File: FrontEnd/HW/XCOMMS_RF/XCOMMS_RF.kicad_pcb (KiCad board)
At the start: 2 copper layers, 40 x 65 mm, 82 parts, among them J1 SMA, J2 SMA, J3 SFC-110-T2-F-D-A-TR, U1 SIM-14+, U2 HMC788ALP2ETR, U3 HMC952ALP5GE, U4 LMX2572RHAT, U5 HMC788ALP2ETR, U6 AD8031, U7 ADT7310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

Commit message: XCOMMS_RF and XCOMMS_Interface KiCad design updated
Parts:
- C49: value Cap Semi -> 100nF
- C50: value Cap Semi -> 100pF
- C51: value Cap Semi -> 1uF
- R10, R7, R8, R9: value Res3 -> 10k
- R5, R6: value Res3 -> 100k
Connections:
- net Net-(C1-Pad1) renamed /AMP1_Out
- net Net-(C1-Pad2) renamed /TP2_In
- net Net-(C2-Pad1) renamed /TP1_Out
- net Net-(C2-Pad2) renamed /AMP1_In
- net Net-(C29-Pad1) renamed /PLL_Out
- net Net-(FL1-Pad1) renamed /Mixer_Out
- R10 pad 1: Net-(R10-Pad1) -> GND
- R10 pad 2: GND -> Net-(R10-Pad2)
- R7 pad 1: Net-(R7-Pad1) -> /Vdet
- R7 pad 2: /Vdet -> Net-(R7-Pad2)
- R8 pad 1: /Tx_PM -> Net-(R7-Pad2)
- R8 pad 2: Net-(R7-Pad1) -> /Tx_PM
- R9 pad 1: Net-(R10-Pad1) -> Net-(R10-Pad2)
- U6 pad 3: Net-(R10-Pad1) -> Net-(R10-Pad2)
- U6 pad 4: Net-(R7-Pad1) -> Net-(R7-Pad2)
- U6 pad 5: /5V -> +5V
- Y1 pad 1: /LO_EN -> /LocalOscillator/LO_EN
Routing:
- net Net-(R7-Pad1): track 9.87 -> 0.00 mm, vias 2 -> 0
- net /Vdet: track 26.6 -> 36.4 mm, vias 2 -> 4
- net Net-(R10-Pad2): track 0.00 -> 3.07 mm
- net Net-(R10-Pad1): track 3.07 -> 0.00 mm

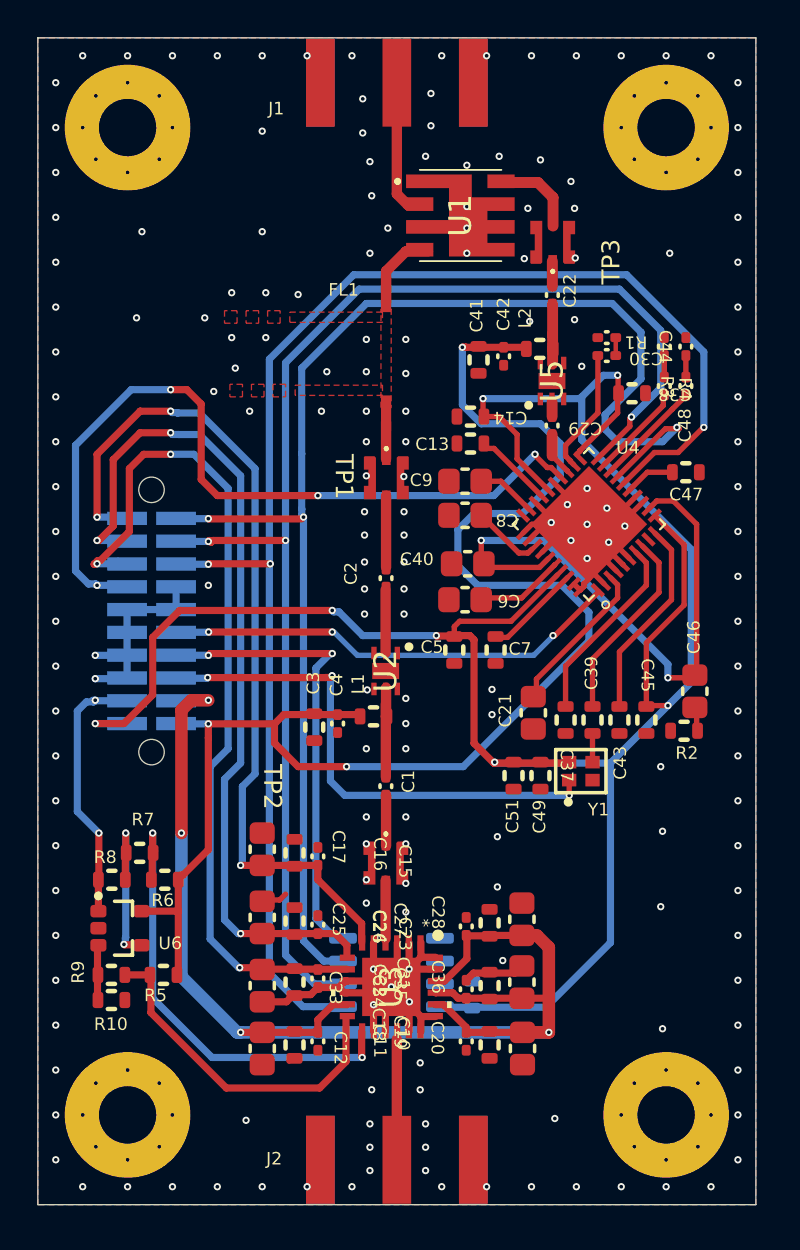
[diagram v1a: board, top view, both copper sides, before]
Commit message: XCOMMS_RF ported to KiCad
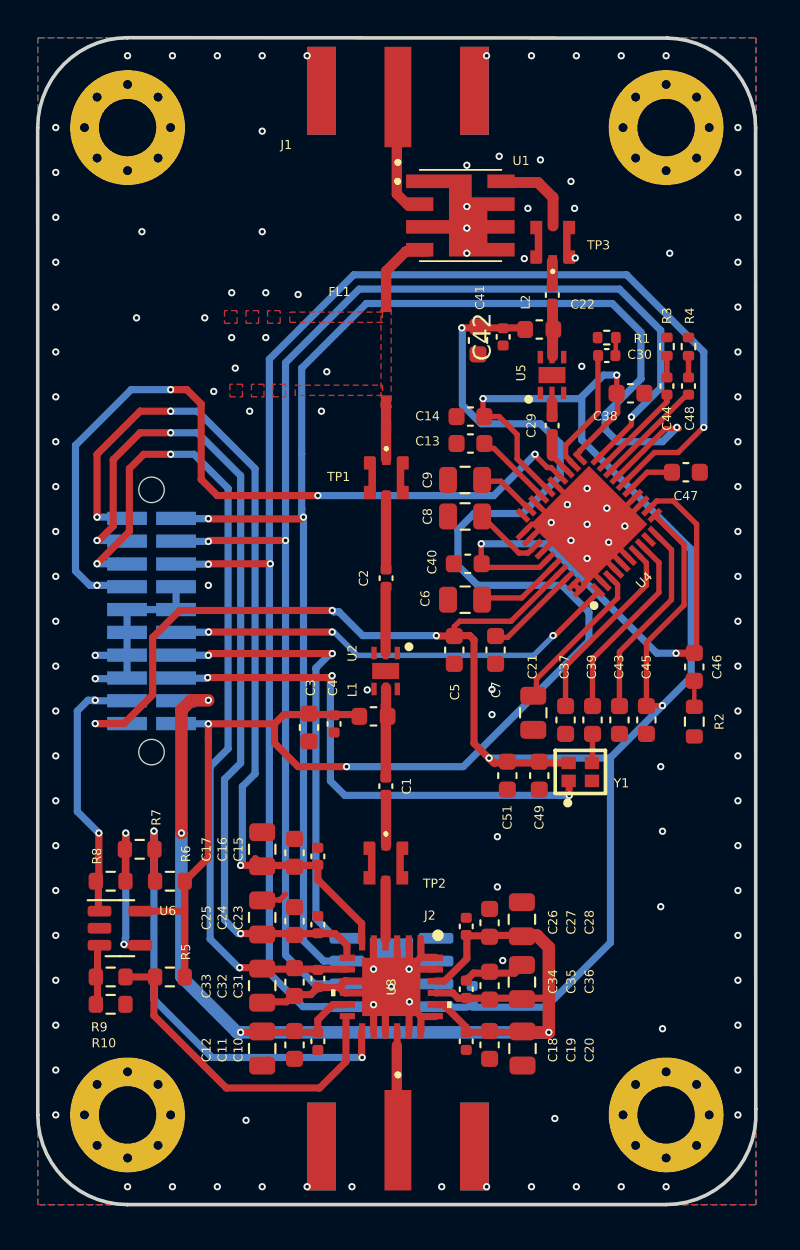
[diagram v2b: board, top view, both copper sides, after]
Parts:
- C1, C10, C15, C18, C2, C22, C23, C26, C31, C34, C4, C42: footprint 3CAT_Miscellaneous.PcbLib:0402 SND CAPACITOR -> Capacitor_SMD:C_0402_1005Metric
- C11, C13, C14, C16, C19, C24, C27, C3, C32, C35, C37, C38, C39, C41, C43, C45, C47, C49, C5, C51, C7: footprint 3CAT_Miscellaneous.PcbLib:0603 SMD Capacitor -> Capacitor_SMD:C_0603_1608Metric
- C12, C17, C20, C21, C25, C28, C33, C36, C6, C8, C9: footprint 3CAT_Miscellaneous.PcbLib:0805 SMD Capacitor -> Capacitor_SMD:C_0805_2012Metric
- C29, C30, C44, C48: value 100nF -> 100pF; footprint 3CAT_Miscellaneous.PcbLib:0402 SND CAPACITOR -> Capacitor_SMD:C_0402_1005Metric
- C40, C46: footprint 3CAT_Miscellaneous.PcbLib:0805 SMD Capacitor -> Capacitor_SMD:C_0603_1608Metric
- C50: footprint 3CAT_Miscellaneous.PcbLib:0603 SMD Capacitor -> Capacitor_SMD:C_0402_1005Metric
- J1, J2: footprint Connectors_GGS.PcbLib:CONSMA020-062-G -> GGS_Connectors:LINX_CONSMA020.062-G
- J3: footprint Connectors_GGS.PcbLib:SAMTEC_SFC-110-T2-F-D-A-TR -> GGS_Connectors:SAMTEC_SFC-110-T2-F-D-A-TR
- L1, L2: footprint 3CAT_Miscellaneous.PcbLib:0603 SMD Inductor -> Inductor_SMD:L_0603_1608Metric
- R1, R3, R4: footprint 3CAT_Miscellaneous.PcbLib:0402 SMD Resistor -> Resistor_SMD:R_0402_1005Metric
- R10, R2, R5, R6, R7, R8, R9: footprint 3CAT_Miscellaneous.PcbLib:0603 SMD Resistor -> Resistor_SMD:R_0603_1608Metric
- SCRW1, SCRW2, SCRW3, SCRW4: footprint 3CAT_Miscellaneous.PcbLib:M3 ScrewHole -> MountingHole:MountingHole_3.2mm_M3_Pad_Via
- U4: footprint RF_GGS.PcbLib:QFN50P600X600X100-41N -> SamacSys_Footprints:QFN50P600X600X100-41N-D
- U6: footprint 3CAT_Miscellaneous.PcbLib:SOT-23-5 -> Package_TO_SOT_SMD:SOT-23-5
- U7: footprint 3CAT_Miscellaneous.PcbLib:SOIC-8 -> Package_SO:SOIC-8-1EP_3.9x4.9mm_P1.27mm_EP2.41x3.81mm
- Y1: footprint Miscellaneous_GGS.PcbLib:ECS-TXO-2016 -> GGS_Miscellaneous:TCXO_ECS
- moved Y1 5.12 mm to (162.2, 117.0)
- moved J1 4.65 mm to (152.7, 72.1)
- moved J2 4.65 mm to (152.7, 135.8)
- moved C46 1.36 mm to (169.2, 106.6)
- moved C42 1.08 mm to (158.6, 88.2)
- moved C41 1.08 mm to (157.2, 88.4)
- moved L2 1.08 mm to (160.6, 87.8)
- moved R2 0.76 mm to (169.2, 109.7), turned to -90 degrees
- moved R5 0.38 mm to (140.0, 123.9)
- moved C51 0.34 mm to (158.8, 112.7)
- moved U5 0.33 mm to (161.3, 90.3)
- moved R6 0.30 mm to (140.0, 118.5)
- moved C3 0.29 mm to (147.8, 110.0)
- moved R10 0.24 mm to (136.7, 125.4), turned to 180 degrees
- moved C4 0.20 mm to (149.1, 109.8)
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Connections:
- net Net-(C13-Pad2) renamed /LocalOscillator/VBIASVCO2
- net Net-(C21-Pad2) renamed /LocalOscillator/VBIASVCO
- net Net-(C22-Pad1) renamed /AMP2_Out
- net Net-(C22-Pad2) renamed /TP3_In
- net Net-(C30-Pad2) renamed /LocalOscillator/RFOUTAM
- net Net-(C39-Pad2) renamed /LocalOscillator/OSCINP
- net Net-(C40-Pad2) renamed /LocalOscillator/VTune
- net Net-(C43-Pad2) renamed /LocalOscillator/OSCINM
- net Net-(C44-Pad2) renamed /LocalOscillator/RFOUTBP
- net Net-(C48-Pad2) renamed /LocalOscillator/RFOUTBM
- net Net-(C6-Pad2) renamed /LocalOscillator/VREFVCO
- net Net-(C8-Pad2) renamed /LocalOscillator/VBIASVARAC
- net Net-(C9-Pad2) renamed /LocalOscillator/VREFVCO2
- net Net-(R10-Pad2) renamed /AD8031_IN+
- net Net-(R7-Pad2) renamed /AD8031_IN-
- C29 pad 1: /PLL_Out -> /LocalOscillator/RFOUTAP
- C29 pad 2: Net-(C29-Pad2) -> /PLL_Out
- U4 pad 23: Net-(C29-Pad2) -> /LocalOscillator/RFOUTAP
- Y1 pad 1: /LocalOscillator/LO_EN -> /LO_EN
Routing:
- net /AD8031_IN-: track 0.00 -> 9.87 mm, vias 0 -> 2
- net /Vdet: track 36.4 -> 26.6 mm, vias 4 -> 2
- net /LocalOscillator/VTune: track 32.7 -> 30.2 mm
- net Net-(C29-Pad2): track 2.39 -> 0.00 mm
- net /LocalOscillator/RFOUTAP: track 0.00 -> 2.39 mm
- net +5V: track 83.7 -> 85.0 mm
- net GND: track 81.6 -> 80.7 mm, vias 219 -> 125
- net Net-(C46-Pad1): track 1.46 -> 0.95 mm
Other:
- outline, holes or cut-outs redrawn

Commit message: XCOMS_RF updated
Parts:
- removed FL1: NotchFilter, RF_GGS.PcbLib:Notch_5600to6100MHz
- C21: value 10uF -> 470nF
- C7: value 1uF -> 10nF
- moved C37 2.17 mm to (159.9, 109.6), turned to 0 degrees
- moved C5 1.81 mm to (156.6, 104.0), turned to 0 degrees
- moved C7 1.75 mm to (159.9, 105.5), turned to 0 degrees
- moved C21 1.70 mm to (159.6, 107.6), turned to 0 degrees
- moved TP3 1.38 mm to (166.4, 83.6)
- moved R1 0.92 mm to (165.1, 88.8), turned to -90 degrees
- moved C22 0.92 mm to (162.2, 85.6), turned to 45 degrees
- moved C40 0.78 mm to (156.6, 100.1)
- moved C6 0.75 mm to (156.5, 102.1)
- moved C30 0.70 mm to (163.8, 88.8), turned to -90 degrees
- moved C47 0.25 mm to (168.8, 96.0), turned to 90 degrees
- moved L1 0.09 mm to (151.3, 109.3)
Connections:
- net /Tx_CE renamed /PLL_CE
- net Net-(C7-Pad2) renamed /LocalOscillator/VREGVCO
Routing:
- net +3V3: track 147.5 -> 154.1 mm, vias 7 -> 8
- net /SDI: track 78.6 -> 76.4 mm
- net /AMP1_Out: track 5.69 -> 3.56 mm
- net /Vdet: track 26.6 -> 28.7 mm
- net /Mixer_Out: track 6.63 -> 4.79 mm
- net /Vref: track 18.8 -> 17.1 mm, vias 0 -> 2
- net /SCK: track 82.6 -> 81.5 mm
- net /AMP1_In: track 3.50 -> 2.41 mm
- net /TP2_In: track 2.83 -> 1.76 mm
- net GND: track 80.7 -> 81.8 mm, vias 125 -> 89
- net /Vd_PA: track 74.1 -> 73.1 mm
- net /TP1_Out: track 4.00 -> 3.05 mm
- net /LocalOscillator/VTune: track 30.2 -> 29.3 mm
- net /LocalOscillator/VREGVCO: track 5.39 -> 4.52 mm
- net /TP3_In: track 1.44 -> 0.76 mm
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
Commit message: XCOMMS_RF update
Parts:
- added FL1: HFCW-7000+, GGS_RF:JC0603C, F.Cu at (152.7, 88.8)
- moved C30 2.16 mm to (163.8, 90.9)
- moved C38 2.11 mm to (166.0, 89.3), turned to -90 degrees
- moved R1 1.27 mm to (163.8, 88.8), turned to 90 degrees
- moved C22 0.64 mm to (161.7, 86.0)
- moved C46 0.56 mm to (169.2, 106.0)
- moved TP3 0.38 mm to (166.0, 83.6)
- moved R7 0.20 mm to (138.3, 117.0)
- moved R2 0.18 mm to (169.2, 109.5)
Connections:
- net /RF_Tx_in renamed /RF_in
- net /RF_Tx_out renamed /RF_out
- TP1 pad 1: /Mixer_Out -> /FL_Out
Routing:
- net GND: track 81.8 -> 70.6 mm, vias 89 -> 88
- net /PLL_CSB: track 45.0 -> 36.4 mm
- net /FL_Out: track 0.00 -> 4.77 mm
- net /Vg_PA1: track 48.3 -> 43.7 mm
- net /Vg_PA2: track 47.8 -> 44.4 mm
- net /SDI: track 76.4 -> 73.5 mm
- net /SDO: track 75.5 -> 73.0 mm
- net /LocalOscillator/RFOUTAM: track 6.72 -> 4.29 mm
- net /Vg_PA3: track 47.7 -> 45.4 mm
- net /Tx_PM: track 15.0 -> 12.8 mm
- net /T_CSB: track 25.9 -> 23.9 mm
- net /SCK: track 81.5 -> 79.8 mm
- net /TP3_In: track 0.76 -> 2.24 mm
- net /Vdet: track 28.7 -> 27.5 mm
- net /PLL_CE: track 25.5 -> 26.6 mm
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- removed copper zone on F.Cu, net (none)
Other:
- board text added: "ROGERS 4350B Layers = 2 Metalization = 35 um Thinkness = 0.762 mm (30 mils) Er = 3.66 tand = 0.0037"

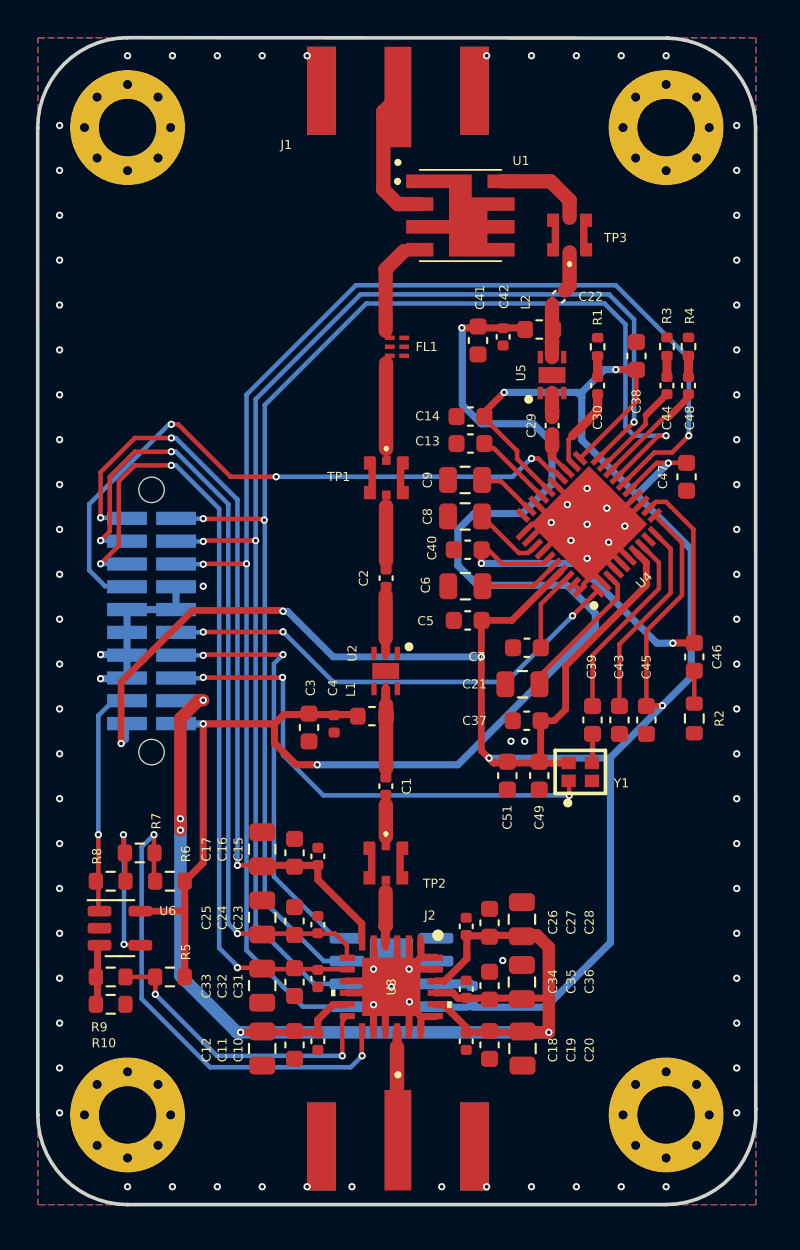
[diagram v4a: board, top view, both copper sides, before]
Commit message: Relaxed Design RUles and output files generated
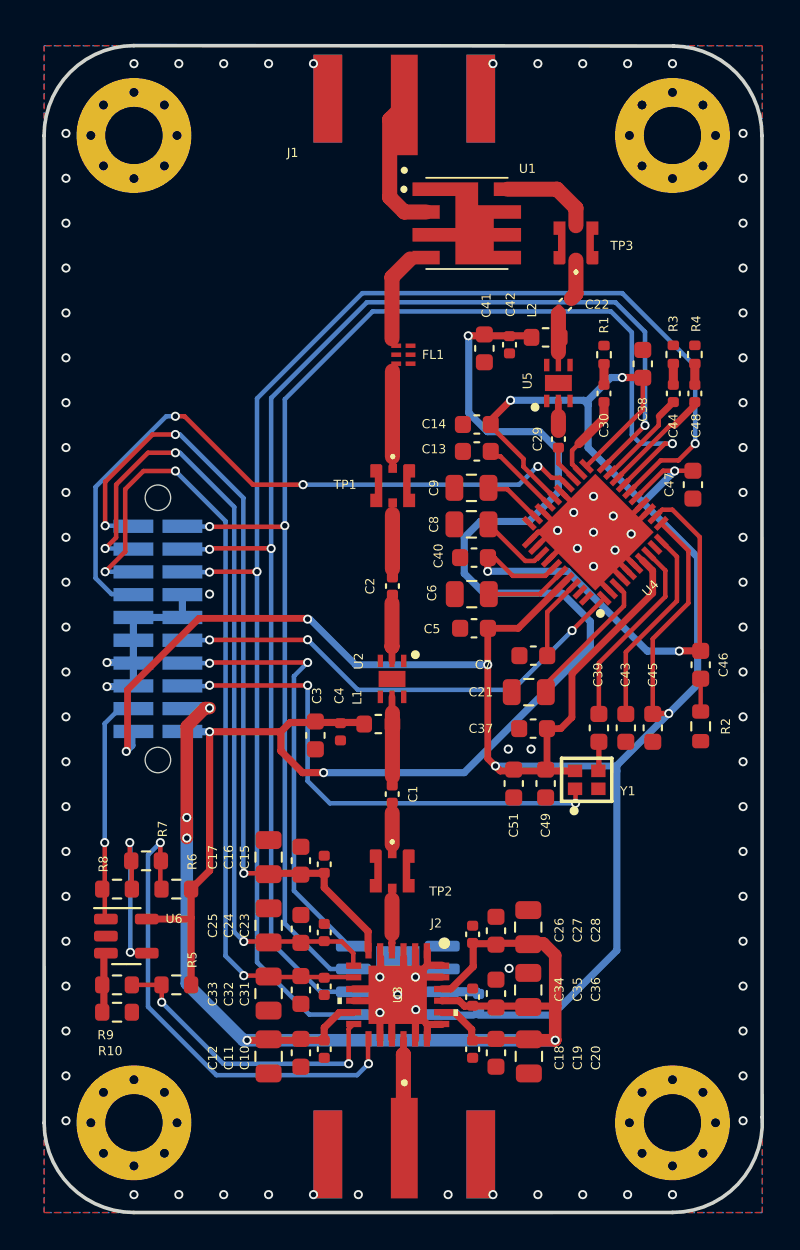
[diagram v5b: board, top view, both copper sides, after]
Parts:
- moved C29 0.83 mm to (161.6, 93.9)
- moved C2 0.57 mm to (152.4, 102.1)
- moved R6 0.57 mm to (140.4, 119.0)
- moved C16 0.57 mm to (147.3, 117.4)
- moved C24 0.57 mm to (147.3, 121.2)
- moved C27 0.57 mm to (158.2, 121.3)
- moved C35 0.57 mm to (158.2, 124.8)
- moved C41 0.57 mm to (157.5, 88.9)
- moved C47 0.57 mm to (169.1, 96.5)
- moved C8 0.57 mm to (156.8, 98.7)
- moved C9 0.57 mm to (156.8, 96.6)
- moved J3 0.57 mm to (139.3, 104.5)
- moved R5 0.57 mm to (140.4, 124.3)
- moved R7 0.57 mm to (138.7, 117.4)
- moved U1 0.57 mm to (156.5, 81.9)
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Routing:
- net GND: track 70.6 -> 68.7 mm
- net /PLL_CSB: track 36.4 -> 37.9 mm
- net /Vg_PA1: track 43.7 -> 44.7 mm
- net +5V: track 84.4 -> 83.5 mm
- net /LocalOscillator/RFOUTAP: track 2.51 -> 1.71 mm
- net /AMP2_Out: track 2.86 -> 2.16 mm
- net /PA_RF_IN: track 2.85 -> 3.50 mm
- net /FL_Out: track 4.77 -> 5.42 mm
- net /AMP1_Out: track 4.45 -> 5.08 mm
- net /LO_EN: track 28.3 -> 28.9 mm
- net /Vg_PA2: track 44.4 -> 45.0 mm
- net /T_CSB: track 23.9 -> 24.4 mm
- net /Vd_PA: track 74.0 -> 74.5 mm
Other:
- board text added: "ROGERS 4350B Layers = 2 Metalization = 35 um Thinkness = 0.508 mm (20 mils) Er = 3.66 tand = 0.0037"
- board text removed: "ROGERS 4350B Layers = 2 Metalization = 35 um Thinkness = 0.762 mm (30 mils) Er = 3.66 tand = 0.0037"

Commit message: changes
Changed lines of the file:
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@@
     (fp_line (start -0.14058 0.51) (end 0.14058 0.51) (layer "F.SilkS") (width 0.12))
     (fp_line (start -0.14058 -0.51) (end 0.14058 -0.51) (layer "F.SilkS") (width 0.12))
+    (fp_line (start -1.48 -0.73) (end 1.48 -0.73) (layer "F.CrtYd") (width 0.05))
     (fp_line (start -1.48 0.73) (end -1.48 -0.73) (layer "F.CrtYd") (width 0.05))
-    (fp_line (start 1.48 -0.73) (end 1.48 0.73) (layer "F.CrtYd") (width 0.05))
     (fp_line (start 1.48 0.73) (end -1.48 0.73) (layer "F.CrtYd") (width 0.05))
-    (fp_line (start -1.48 -0.73) (end 1.48 -0.73) (layer "F.CrtYd") (width 0.05))
+    (fp_line (start 1.48 -0.73) (end 1.48 0.73) (layer "F.CrtYd") (width 0.05))
     (fp_line (start -0.8 0.4) (end -0.8 -0.4) (layer "F.Fab") (width 0.1))
-    (fp_line (start -0.8 -0.4) (end 0.8 -0.4) (layer "F.Fab") (width 0.1))
     (fp_line (start 0.8 -0.4) (end 0.8 0.4) (layer "F.Fab") (width 0.1))
+    (fp_line (start -0.8 -0.4) (end 0.8 -0.4) (layer "F.Fab") (width 0.1))
     (fp_line (start 0.8 0.4) (end -0.8 0.4) (layer "F.Fab") (width 0.1))
     (pad "1" smd roundrect (at -0.775 0 270) (size 0.9 0.95) (layers "F.Cu" "F.Paste" "F.Mask") (roundrect_rratio 0.25)
@@
   (segment (start 147.420998 96.452) (end 144.626998 96.452) (width 0.254) (layer "F.Cu") (net 14))
   (segment (start 140.816998 92.642) (end 140.308998 92.642) (width 0.254) (layer "F.Cu") (net 14))
-  (segment (start 160.62623 95.436) (end 161.26123 96.071) (width 0.254) (layer "F.Cu") (net 14))
-  (segment (start 161.26123 96.071) (end 161.731669 96.071) (width 0.254) (layer "F.Cu") (net 14))
-  (segment (start 144.626998 96.452) (end 140.816998 92.642) (width 0.254) (layer "F.Cu") (net 14))
-  (segment (start 161.731669 96.071) (end 162.144375 96.483706) (width 0.254) (layer "F.Cu") (net 14))
+  (segment (start 161.20223 96.012) (end 161.672669 96.012) (width 0.254) (layer "F.Cu") (net 14))
+  (segment (start 160.62623 95.436) (end 161.20223 96.012) (width 0.254) (layer "F.Cu") (net 14))
   (segment (start 160.501998 95.436) (end 160.62623 95.436) (width 0.254) (layer "F.Cu") (net 14))
+  (segment (start 144.626998 96.452) (end 140.816998 92.642) (width 0.254) (layer "F.Cu") (net 14))
+  (segment (start 161.672669 96.012) (end 162.144375 96.483706) (width 0.254) (layer "F.Cu") (net 14))
   (via (at 160.501998 95.436) (size 0.508) (drill 0.3048) (layers "F.Cu" "B.Cu") (net 14))
   (via (at 140.308998 92.642) (size 0.508) (drill 0.3048) (layers "F.Cu" "B.Cu") (net 14))

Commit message: PA TB
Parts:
- SCRW1: footprint MountingHole:MountingHole_3.2mm_M3_Pad_Via -> MountingHole:MountingHole_2.7mm_M2.5_Pad_Via
- SCRW2, SCRW3, SCRW4: footprint MountingHole:MountingHole_3.2mm_M3_Pad_Via -> MountingHole:MountingHole_2.7mm_Pad_Via

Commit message: XCOMMS RF update and PA EvalBoard
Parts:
- J1, J2: value SMA -> SMP-MSLD-PCE-5T; footprint GGS_Connectors:LINX_CONSMA020.062-G -> GGS_Connectors:SMP-MSLD-PCE-5T
- SCRW1: footprint MountingHole:MountingHole_2.7mm_M2.5_Pad_Via -> MountingHole:MountingHole_2.7mm_M2.5_ISO14580_Pad
- SCRW2, SCRW3, SCRW4: footprint MountingHole:MountingHole_2.7mm_Pad_Via -> MountingHole:MountingHole_2.7mm_M2.5_ISO14580_Pad
- moved J1 57.9 mm to (153.0, 130.4), turned to 90 degrees
- moved J2 57.6 mm to (153.0, 78.6), turned to -90 degrees
- moved SCRW2 2.83 mm to (136.0, 75.0)
- moved SCRW1 2.83 mm to (136.0, 134.0)
- moved SCRW4 2.83 mm to (170.0, 75.0)
- moved SCRW3 2.83 mm to (170.0, 134.0)
- moved TP3 2.20 mm to (167.0, 86.2)
- moved U1 2.20 mm to (157.2, 84.0)
- moved C42 1.96 mm to (158.8, 90.6)
- moved L2 1.96 mm to (160.8, 90.2)
- moved U4 1.95 mm to (163.7, 101.1)
- moved C13 1.95 mm to (157.1, 96.6)
- moved C14 1.95 mm to (157.1, 95.1)
- moved C21 1.95 mm to (160.0, 110.0)
- moved C30 1.95 mm to (164.2, 93.3)
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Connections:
- J1 pad 1: /RF_in -> /RF_out
- J2 pad 1: /RF_out -> /RF_in
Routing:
- net +5V: track 83.5 -> 66.0 mm
- net /RF_out: track 7.49 -> 3.62 mm
- net /SDI: track 73.6 -> 76.0 mm
- net /SDO: track 73.3 -> 75.6 mm
- net GND: track 68.7 -> 66.6 mm, vias 88 -> 190
- net /LO_EN: track 28.9 -> 30.7 mm
- net /RF_in: track 7.85 -> 6.08 mm
- net /SCK: track 79.9 -> 81.6 mm
- net /PLL_CE: track 26.6 -> 27.7 mm
- net +3V3: track 154.3 -> 153.3 mm
- net /Mixer_Out: track 4.87 -> 3.90 mm
- net /AMP2_Out: track 2.16 -> 2.86 mm
- net /Vg_PA3: track 45.5 -> 44.8 mm
- net /Tx_PM: track 12.8 -> 12.1 mm
- net /Vg_PA2: track 45.0 -> 44.4 mm
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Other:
- outline, holes or cut-outs redrawn
